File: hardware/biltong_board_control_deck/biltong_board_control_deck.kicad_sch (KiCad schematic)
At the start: 26 parts, among them J1 SH1122_DISP, J2 BILTONG_BOARD, Q1 MMBT3904, SW1 UP, SW2 ENTER, SW3 DOWN

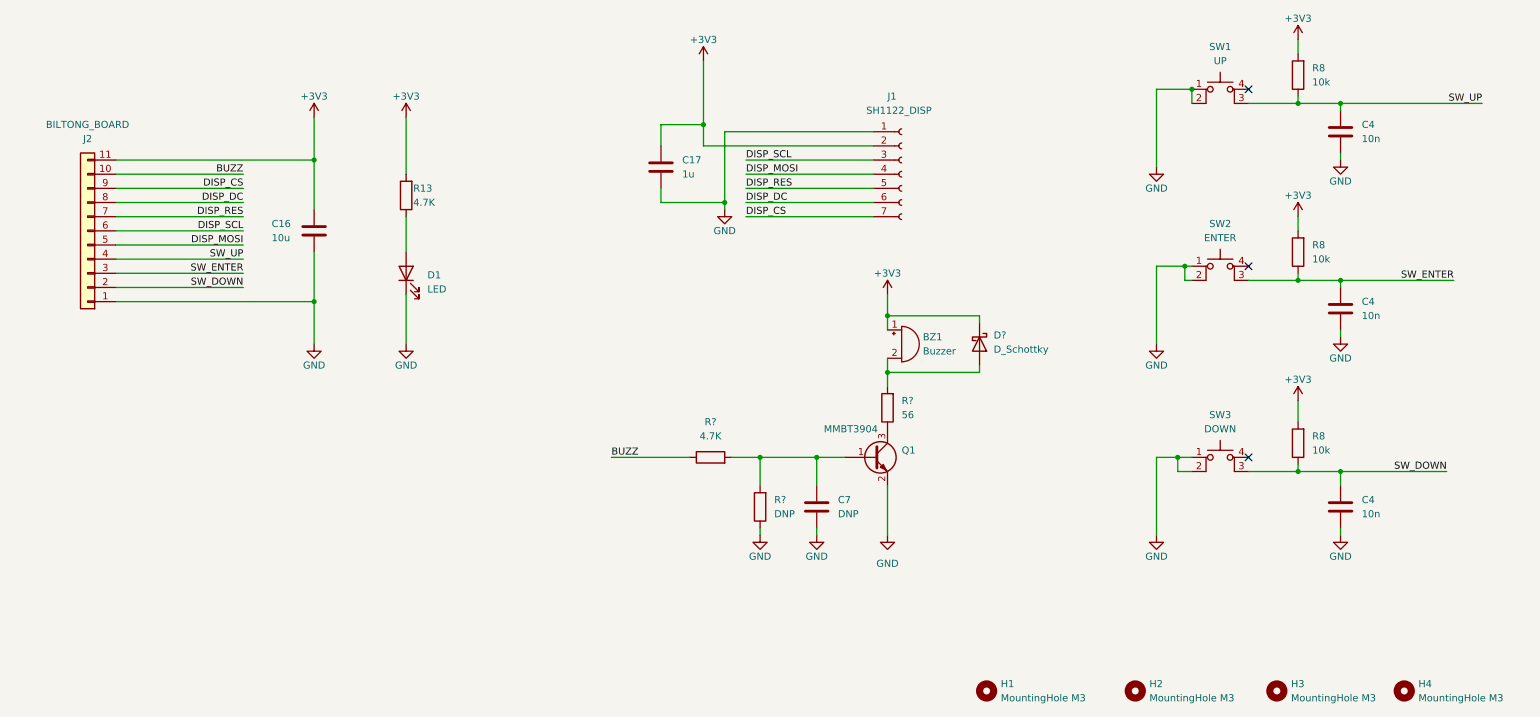
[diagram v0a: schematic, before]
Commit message: generated BOM, swapped 10u cap size, README.md changes
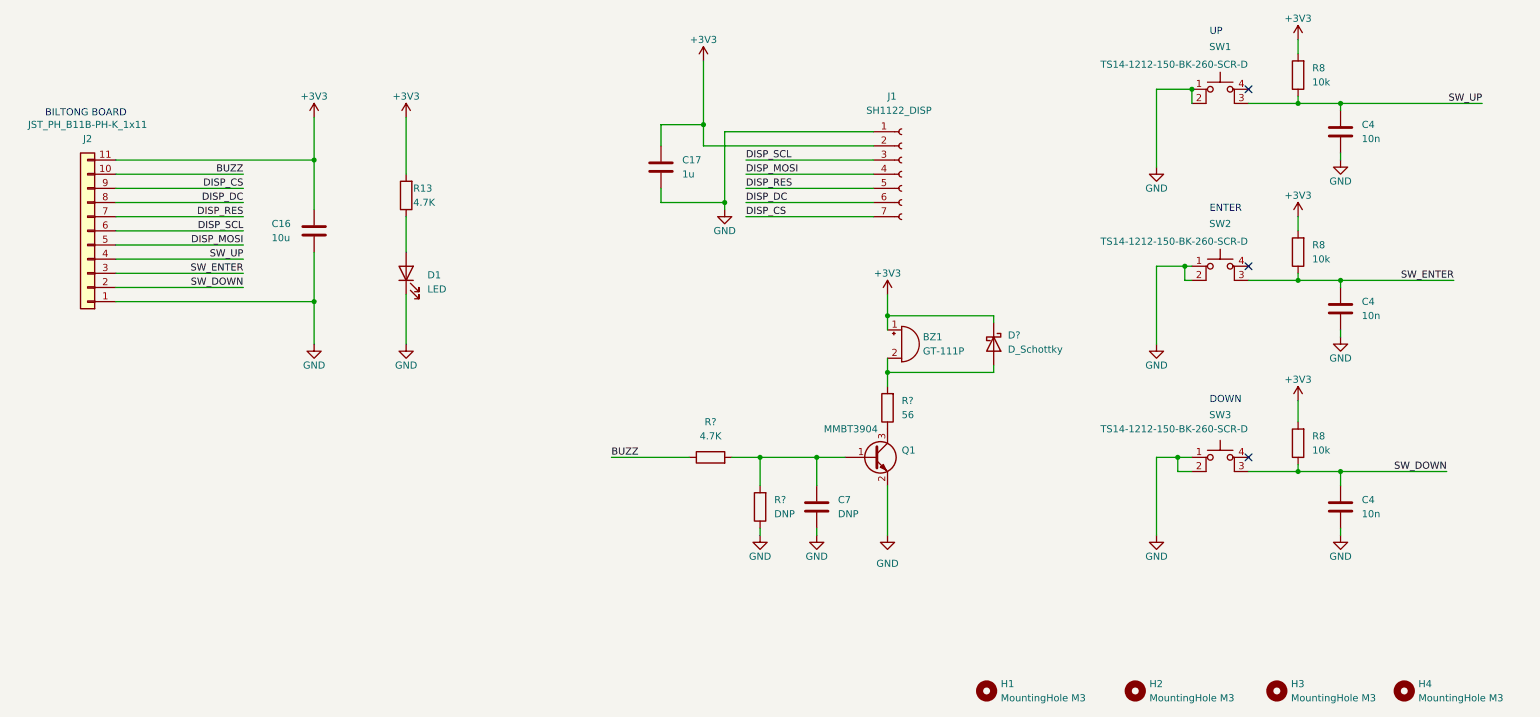
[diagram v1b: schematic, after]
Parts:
- BZ1: value Buzzer -> GT-111P
- C16: footprint Capacitor_THT:CP_Radial_D4.0mm_P2.00mm -> Capacitor_THT:CP_Radial_D5.0mm_P2.00mm
- H1, H2, H3, H4: now left out of the parts list
- J2: value BILTONG_BOARD -> JST_PH_B11B-PH-K_1x11
- SW1: value UP -> TS14-1212-150-BK-260-SCR-D
- SW2: value ENTER -> TS14-1212-150-BK-260-SCR-D
- SW3: value DOWN -> TS14-1212-150-BK-260-SCR-D
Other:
- note added: "BILTONG BOARD"
- note added: "DOWN"
- note added: "ENTER"
- note added: "UP"
- moved on the sheet: D?
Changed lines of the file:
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@@
   (no_connect (at 233.68 66.04))
   (no_connect (at 233.68 34.29))
-  (wire (pts (xy 185.42 76.2) (xy 185.42 74.93))
+  (wire (pts (xy 187.96 76.2) (xy 187.96 74.93))
     (stroke (width 0) (type default))
   )
@@
     (stroke (width 0) (type default))
   )
-  (wire (pts (xy 185.42 74.93) (xy 168.91 74.93))
+  (wire (pts (xy 187.96 74.93) (xy 168.91 74.93))
     (stroke (width 0) (type default))
   )
@@
     (stroke (width 0) (type default))
   )
-  (wire (pts (xy 185.42 83.82) (xy 185.42 85.09))
+  (wire (pts (xy 187.96 83.82) (xy 187.96 85.09))
     (stroke (width 0) (type default))
   )
@@
     (stroke (width 0) (type default))
   )
-  (wire (pts (xy 185.42 85.09) (xy 168.91 85.09))
+  (wire (pts (xy 187.96 85.09) (xy 168.91 85.09))
     (stroke (width 0) (type default))
   )
   (wire (pts (xy 139.7 54.61) (xy 139.7 55.88))
     (stroke (width 0) (type default))
+  )
+  (text "DOWN" (at 226.695 90.805 0)
+    (effects (font (size 1.27 1.27)) (justify left bottom))
+  )
+  (text "BILTONG BOARD" (at 17.78 39.37 0)
+    (effects (font (size 1.27 1.27)) (justify left bottom))
+  )
+  (text "ENTER" (at 226.695 56.515 0)
+    (effects (font (size 1.27 1.27)) (justify left bottom))
+  )
+  (text "UP" (at 226.695 24.765 0)
+    (effects (font (size 1.27 1.27)) (justify left bottom))
   )
   (label "DISP_SCL" (at 143.51 46.99 0) (fields_autoplaced)
@@
       (effects (font (size 1.27 1.27)) (justify left))
     )
-    (property "Footprint" "Capacitor_THT:CP_Radial_D4.0mm_P2.00mm" (at 67.0052 63.5 0)
+    (property "Footprint" "Capacitor_THT:CP_Radial_D5.0mm_P2.00mm" (at 67.0052 63.5 0)
       (effects (font (size 1.27 1.27)) hide)
     )
@@
   )
   (symbol (lib_id "Mechanical:MountingHole") (at 261.62 142.24 0) (unit 1)
-    (in_bom yes) (on_board yes) (dnp no) (fields_autoplaced)
+    (in_bom no) (on_board yes) (dnp no) (fields_autoplaced)
     (property "Reference" "H4" (at 264.16 140.97 0)
       (effects (font (size 1.27 1.27)) (justify left))
@@
   )
   (symbol (lib_id "Mechanical:MountingHole") (at 213.36 142.24 90) (unit 1)
-    (in_bom yes) (on_board yes) (dnp no) (fields_autoplaced)
+    (in_bom no) (on_board yes) (dnp no) (fields_autoplaced)
     (property "Reference" "H2" (at 215.9 140.97 90)
       (effects (font (size 1.27 1.27)) (justify right))
@@
   )
   (symbol (lib_id "Switch:SW_MEC_5E") (at 228.6 102.87 0) (unit 1)
-    (in_bom yes) (on_board yes) (dnp no) (fields_autoplaced)
+    (in_bom yes) (on_board yes) (dnp no)
     (property "Reference" "SW3" (at 228.6 92.71 0)
       (effects (font (size 1.27 1.27)))
     )
-    (property "Value" "DOWN" (at 228.6 95.25 0)
+    (property "Value" "TS14-1212-150-BK-260-SCR-D" (at 220.345 95.25 0)
       (effects (font (size 1.27 1.27)))
     )
@@
       (effects (font (size 1.27 1.27)))
     )
-    (property "Value" "BILTONG_BOARD" (at 25.4 40.64 0)
+    (property "Value" "JST_PH_B11B-PH-K_1x11" (at 25.4 40.64 0)
       (effects (font (size 1.27 1.27)))
     )
@@
   )
   (symbol (lib_id "Switch:SW_MEC_5E") (at 228.6 36.83 0) (unit 1)
-    (in_bom yes) (on_board yes) (dnp no) (fields_autoplaced)
+    (in_bom yes) (on_board yes) (dnp no)
     (property "Reference" "SW1" (at 228.6 26.67 0)
       (effects (font (size 1.27 1.27)))
     )
-    (property "Value" "UP" (at 228.6 29.21 0)
+    (property "Value" "TS14-1212-150-BK-260-SCR-D" (at 220.345 29.845 0)
       (effects (font (size 1.27 1.27)))
     )
@@
   )
   (symbol (lib_id "Mechanical:MountingHole") (at 238.76 142.24 0) (unit 1)
-    (in_bom yes) (on_board yes) (dnp no) (fields_autoplaced)
+    (in_bom no) (on_board yes) (dnp no) (fields_autoplaced)
     (property "Reference" "H3" (at 241.3 140.97 0)
       (effects (font (size 1.27 1.27)) (justify left))
@@
   )
   (symbol (lib_id "Switch:SW_MEC_5E") (at 228.6 68.58 0) (unit 1)
-    (in_bom yes) (on_board yes) (dnp no) (fields_autoplaced)
+    (in_bom yes) (on_board yes) (dnp no)
     (property "Reference" "SW2" (at 228.6 58.42 0)
       (effects (font (size 1.27 1.27)))
     )
-    (property "Value" "ENTER" (at 228.6 60.96 0)
+    (property "Value" "TS14-1212-150-BK-260-SCR-D" (at 220.345 61.595 0)
       (effects (font (size 1.27 1.27)))
     )
@@
       (effects (font (size 1.27 1.27)) (justify left))
     )
-    (property "Value" "Buzzer" (at 175.26 81.28 0)
+    (property "Value" "GT-111P" (at 175.26 81.28 0)
       (effects (font (size 1.27 1.27)) (justify left))
     )
@@
   )
   (symbol (lib_id "Mechanical:MountingHole") (at 186.69 142.24 0) (unit 1)
-    (in_bom yes) (on_board yes) (dnp no) (fields_autoplaced)
+    (in_bom no) (on_board yes) (dnp no) (fields_autoplaced)
     (property "Reference" "H1" (at 189.23 140.97 0)
       (effects (font (size 1.27 1.27)) (justify left))
@@
     )
   )
-  (symbol (lib_id "Device:D_Schottky") (at 185.42 80.01 270) (unit 1)
+  (symbol (lib_id "Device:D_Schottky") (at 187.96 80.01 270) (unit 1)
     (in_bom yes) (on_board yes) (dnp no) (fields_autoplaced)
-    (property "Reference" "D?" (at 187.96 78.4225 90)
-      (effects (font (size 1.27 1.27)) (justify left))
-    )
-    (property "Value" "D_Schottky" (at 187.96 80.9625 90)
-      (effects (font (size 1.27 1.27)) (justify left))
-    )
-    (property "Footprint" "Diode_SMD:D_SOD-323" (at 185.42 80.01 0)
-      (effects (font (size 1.27 1.27)) hide)
-    )
-    (property "Datasheet" "https://www.digikey.com/en/products/detail/micro-commercial-co/SD101AWS-TP/717300" (at 185.42 80.01 0)
-      (effects (font (size 1.27 1.27)) hide)
-    )
+    (property "Reference" "D?" (at 190.5 78.4225 90)
+      (effects (font (size 1.27 1.27)) (justify left))
+    )
+    (property "Value" "D_Schottky" (at 190.5 80.9625 90)
+      (effects (font (size 1.27 1.27)) (justify left))
+    )
+    (property "Footprint" "Diode_SMD:D_SOD-323" (at 187.96 80.01 0)
+      (effects (font (size 1.27 1.27)) hide)
+    )
+    (property "Datasheet" "https://www.digikey.com/en/products/detail/micro-commercial-co/SD101AWS-TP/717300" (at 187.96 80.01 0)
+      (effects (font (size 1.27 1.27)) hide)
+    )

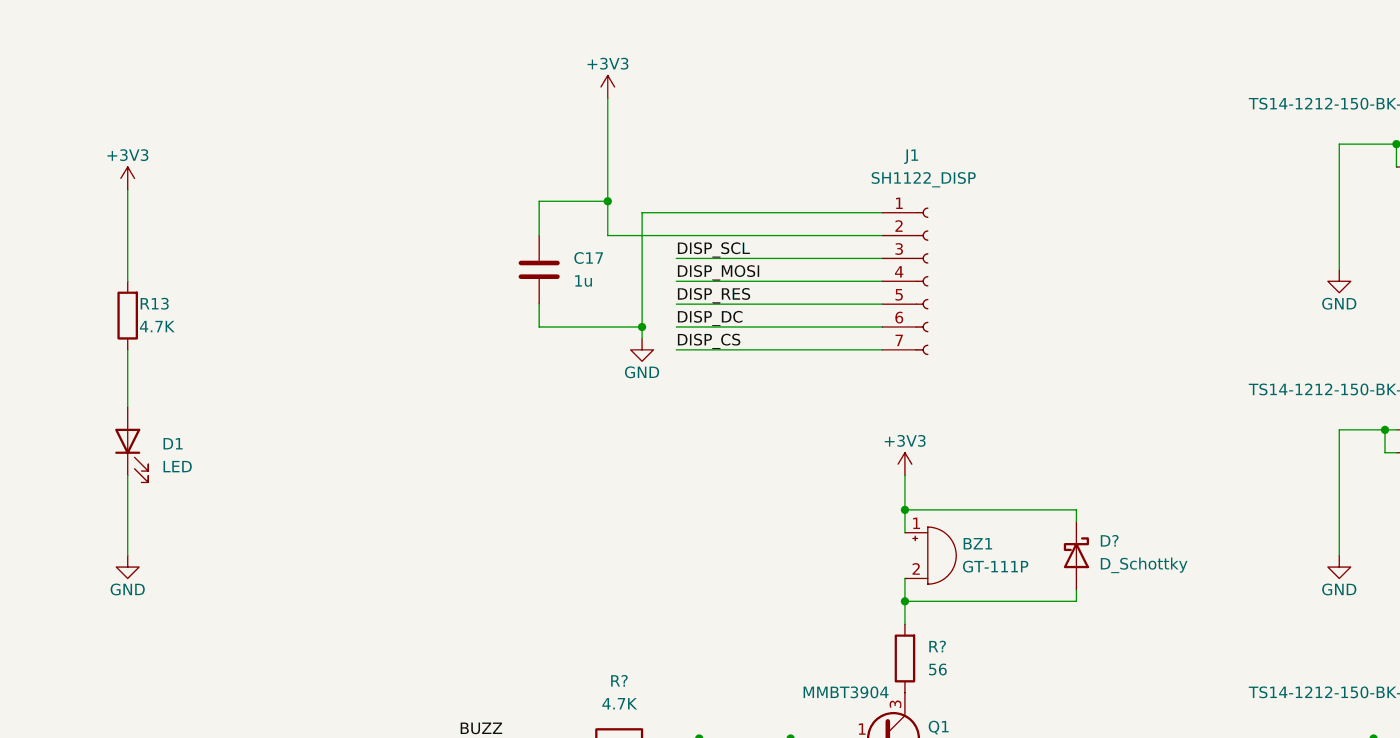
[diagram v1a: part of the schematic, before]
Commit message: corrected control deck schematic values
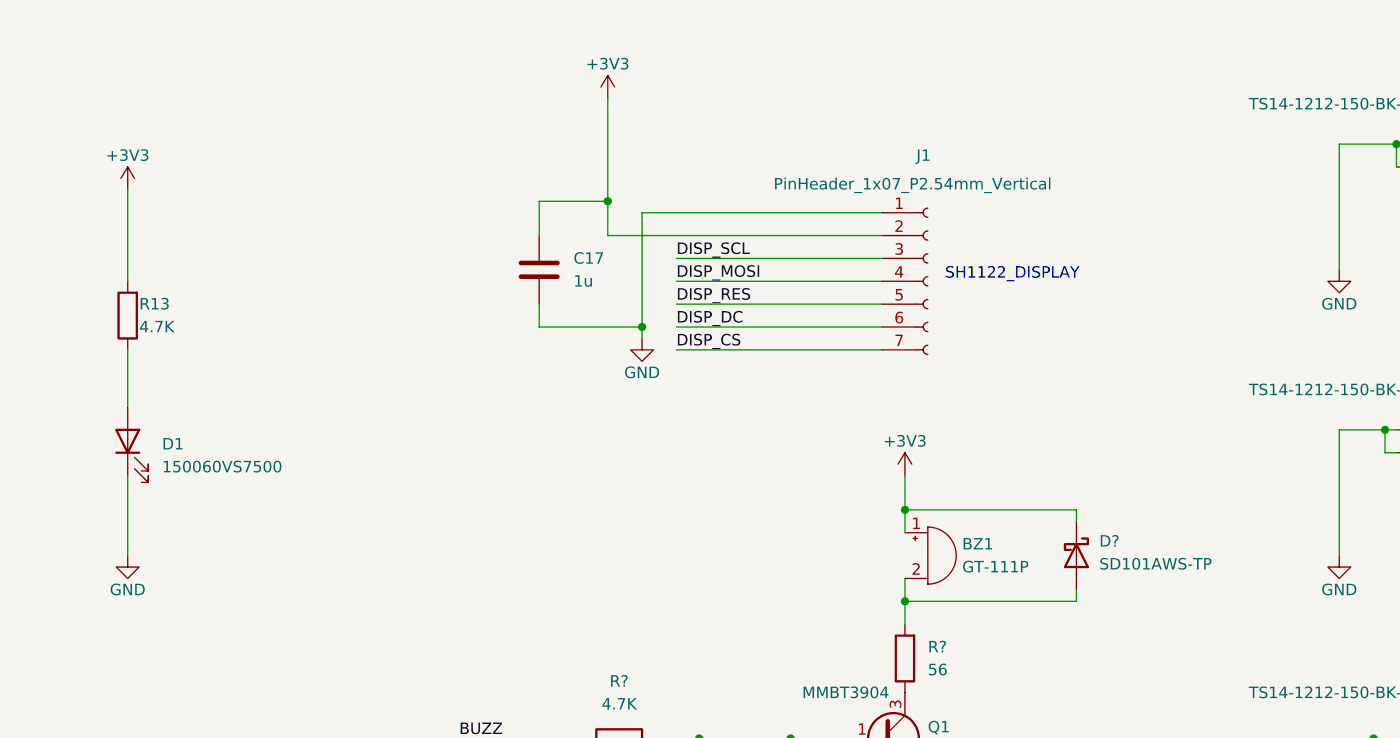
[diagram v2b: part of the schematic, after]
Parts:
- D1: value LED -> 150060VS7500
- D?: value D_Schottky -> SD101AWS-TP
- J1: value SH1122_DISP -> PinHeader_1x07_P2.54mm_Vertical
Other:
- note added: "SH1122_DISPLAY"
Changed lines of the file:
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@@
+    (effects (font (size 1.27 1.27)) (justify left bottom))
+  )
+  (text "SH1122_DISPLAY" (at 173.355 49.53 0)
     (effects (font (size 1.27 1.27)) (justify left bottom))
   )
@@
   (symbol (lib_id "Connector:Conn_01x07_Socket") (at 171.45 49.53 0) (unit 1)
     (in_bom yes) (on_board yes) (dnp no)
-    (property "Reference" "J1" (at 168.91 35.56 0)
-      (effects (font (size 1.27 1.27)) (justify left))
-    )
-    (property "Value" "SH1122_DISP" (at 165.1 38.1 0)
+    (property "Reference" "J1" (at 170.18 35.56 0)
+      (effects (font (size 1.27 1.27)) (justify left))
+    )
+    (property "Value" "PinHeader_1x07_P2.54mm_Vertical" (at 154.305 38.735 0)
       (effects (font (size 1.27 1.27)) (justify left))
     )
@@
       (effects (font (size 1.27 1.27)) (justify left))
     )
-    (property "Value" "D_Schottky" (at 190.5 80.9625 90)
+    (property "Value" "SD101AWS-TP" (at 190.5 80.9625 90)
       (effects (font (size 1.27 1.27)) (justify left))
     )
@@
       (effects (font (size 1.27 1.27)) (justify right))
     )
-    (property "Value" "LED" (at 86.36 70.1675 90)
-      (effects (font (size 1.27 1.27)) (justify right))
-    )
+    (property "Value" "150060VS7500" (at 86.36 70.1675 90)
+      (effects (font (size 1.27 1.27)) (justify right))
+    )
